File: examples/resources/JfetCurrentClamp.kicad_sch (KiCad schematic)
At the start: 3 parts

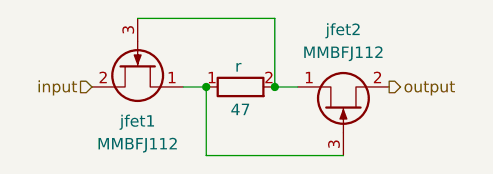
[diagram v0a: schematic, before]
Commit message: fix cap parsing
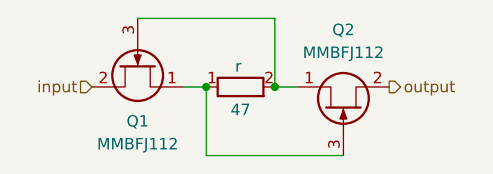
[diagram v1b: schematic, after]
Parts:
- renumbered jfet1 to Q1, jfet2 to Q2
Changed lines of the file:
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@@
 		(dnp no)
 		(fields_autoplaced yes)
-		(property "Reference" "jfet1"
+		(property "Reference" "Q1"
 			(at 115.57 130.81 90)
 			(effects
@@
 			(project ""
 				(path "/b55f6c44-5d5d-4524-bb86-893662f64598"
-					(reference "jfet1")
+					(reference "Q1")
 					(unit 1)
 				)
@@
 		(dnp no)
 		(fields_autoplaced yes)
-		(property "Reference" "jfet2"
+		(property "Reference" "Q2"
 			(at 138.43 120.65 90)
 			(effects
@@
 			(project "JfetCurrentClamp"
 				(path "/b55f6c44-5d5d-4524-bb86-893662f64598"
-					(reference "jfet2")
+					(reference "Q2")
 					(unit 1)
 				)
